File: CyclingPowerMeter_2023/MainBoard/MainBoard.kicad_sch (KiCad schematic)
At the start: 5 parts

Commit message: BLE sample code
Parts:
- removed U?: ESP32-WROOM-32, RF_Module:ESP32-WROOM-32, symbol RF_Module:ESP32-WROOM-32
- removed U?: AD7193BRUZ, SOP65P640X120-28N, symbol AD7193BRUZ:AD7193BRUZ
- added J?: Conn_01x02, symbol Connector_Generic:Conn_01x02
- added J? (x2): Conn_01x01, symbol Connector_Generic:Conn_01x01
- added MOSFET?: SSM3J332R_LF, SOT-23F_TOS, symbol SSM3J332RLF:SSM3J332R_LF
- added U?: ADS122U04IPW, PW0016A_N, symbol ADS122U04IPW:ADS122U04IPW
- added U?: Seeed_Studio_XIAO_nRF52840_Sense, symbol Seeed_Studio_XIAO_nRF52840_Sense:Seeed_Studio_XIAO_nRF52840_Sense
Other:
- moved on the sheet: C?, U?

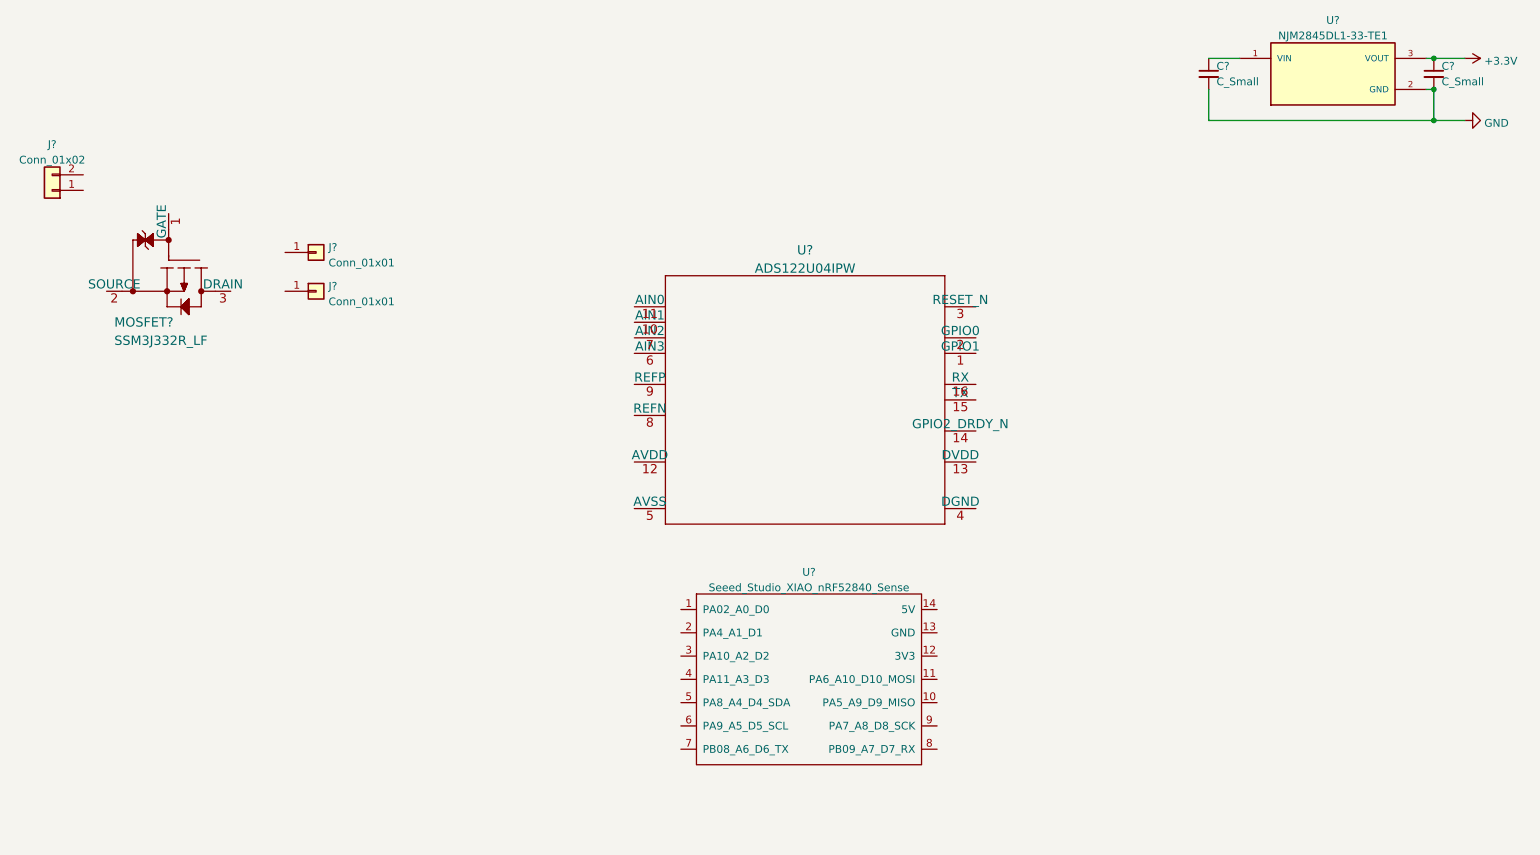
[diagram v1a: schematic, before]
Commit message: パワメの回路図が完成（暫定）
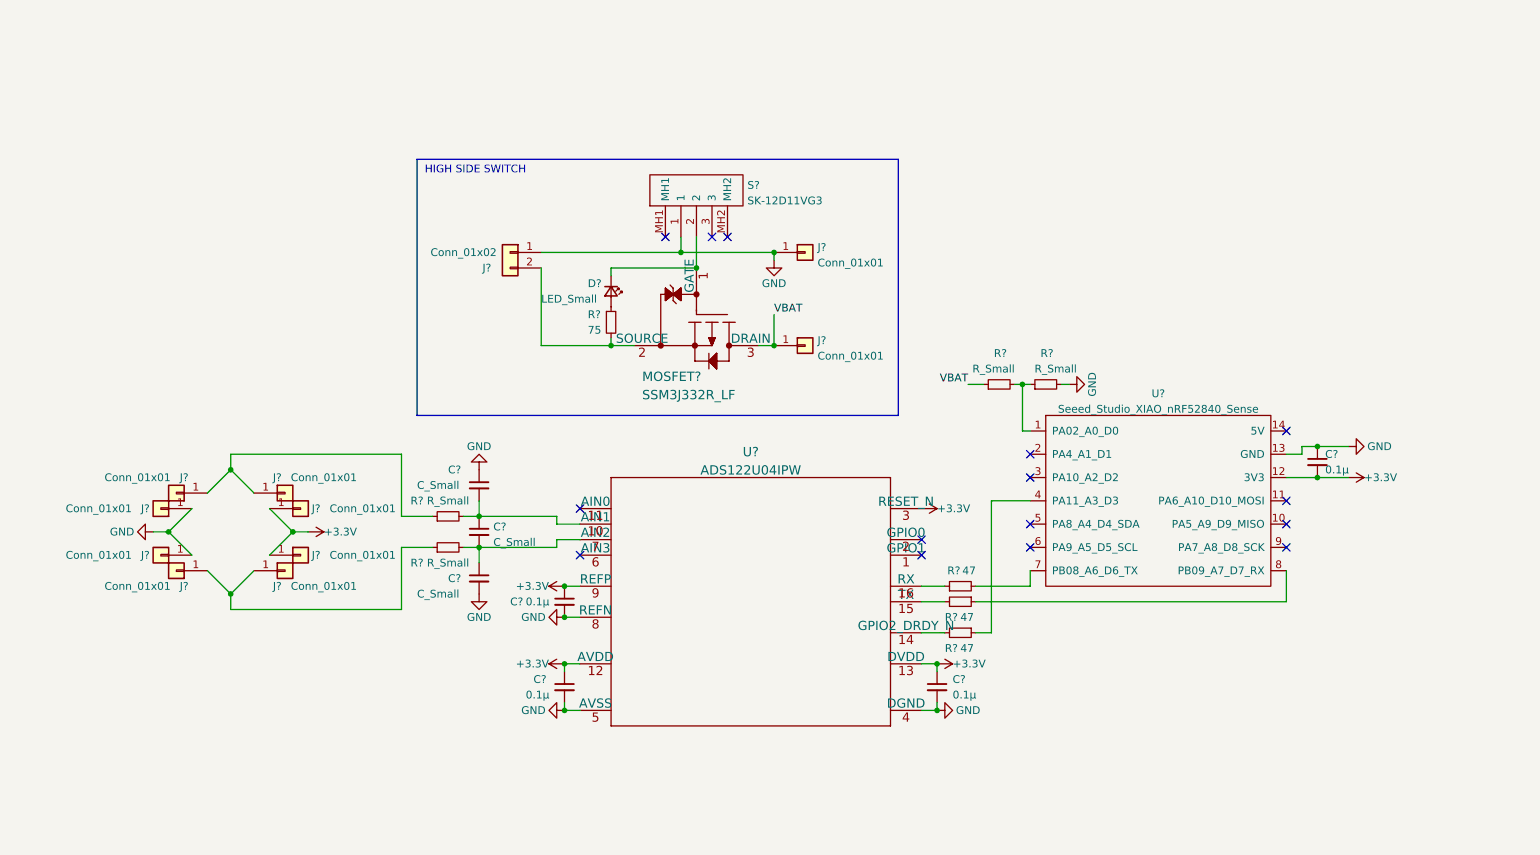
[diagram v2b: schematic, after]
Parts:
- removed C? (x2): C_Small, symbol Device:C_Small
- removed U?: NJM2845DL1-33-TE1, DPAK228P968X238-4N, symbol NJM2845DL1-33-TE1:NJM2845DL1-33-TE1
- added C? (x4): 0.1μ, symbol Device:C_Small
- added C? (x3): C_Small, symbol Device:C_Small
- added D?: LED_Small, symbol Device:LED_Small
- added J? (x8): Conn_01x01, symbol Connector_Generic:Conn_01x01
- added R? (x3): 47, symbol Device:R_Small
- added R?: 75, symbol Device:R_Small
- added R? (x4): R_Small, symbol Device:R_Small
- added S?: SK-12D11VG3, SK12D11VG3, symbol SK-12D11VG3:SK-12D11VG3
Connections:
- net +3.3V: now also U?.12 (3V3), U?.12 (AVDD), U?.13 (DVDD), U?.3 (RESET_N), U?.9 (REFP), C?.1, C?.1, C?.1, C?.2, J?.1 (Pin_1), J?.1 (Pin_1)
- net GND: now also J?.1 (Pin_1), J?.1 (Pin_1), U?.13 (GND), U?.4 (DGND), U?.5 (AVSS), U?.8 (REFN), C?.1, C?.1, C?.2, C?.2, C?.2, C?.2, J?.1 (Pin_1), J?.1 (Pin_1), R?.2, S?.1
- net at U?.10 (AIN1): now also C?.1, C?.2, R?.2
- net at U?.14 (GPIO2_DRDY_N): now also R?.2
- net at U?.15 (TX): now also R?.2
- net at U?.16 (RX): now also R?.1
- net at U?.7 (AIN2): now also C?.1, C?.2, R?.2
- net at J?.2 (Pin_2): now also MOSFET?.2 (SOURCE), R?.2
- net VBAT: now reaches J?.1 (Pin_1)
- net VBAT: now also MOSFET?.3 (DRAIN), R?.1
- net at U?.1 (PA02_A0_D0): now also R?.1, R?.2
- net at U?.4 (PA11_A3_D3): now also R?.1
- net at U?.7 (PB08_A6_D6_TX): now also R?.2
- net at U?.8 (PB09_A7_D7_RX): now also R?.1
- net at MOSFET?.1 (GATE): now also D?.1 (K), S?.2
- new net: D?.2 (A), R?.1
- new net: J?.1 (Pin_1), J?.1 (Pin_1), R?.1 (x2)
- no-connect marks 0 -> 15
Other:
- note added: "HIGH SIDE SWITCH"
- moved on the sheet: J?, MOSFET?, U?

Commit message: フットプリントを割り当て
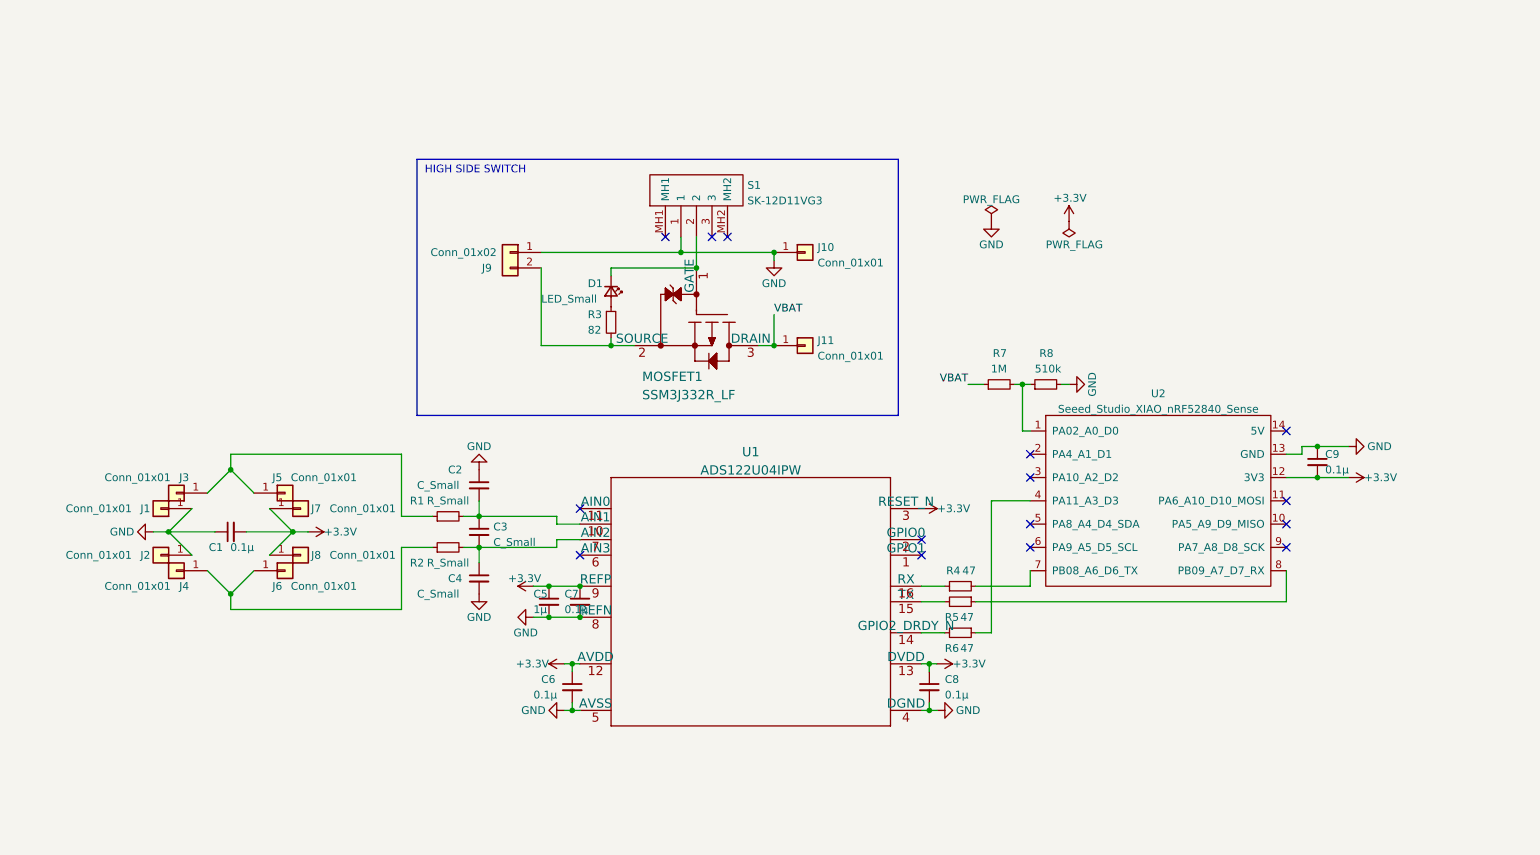
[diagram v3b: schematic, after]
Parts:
- added C1: 0.1μ, Capacitor_SMD:C_0603_1608Metric_Pad1.08x0.95mm_HandSolder, symbol Device:C_Small
- added C5: 1μ, Capacitor_SMD:C_0603_1608Metric_Pad1.08x0.95mm_HandSolder, symbol Device:C_Small
- C2, C3, C4, C6, C7, C8, C9: renamed from C?; footprint (none) -> Capacitor_SMD:C_0603_1608Metric_Pad1.08x0.95mm_HandSolder
- D1: renamed from D?; footprint (none) -> LED_SMD:LED_0603_1608Metric_Pad1.05x0.95mm_HandSolder
- J1, J2, J3, J4, J5, J6, J7, J8: renamed from J?; footprint (none) -> Connector_Wire:SolderWirePad_1x01_SMD_1x2mm
- J10, J11: renamed from J?; footprint (none) -> TestPoint:TestPoint_THTPad_4.0x4.0mm_Drill2.0mm
- J9: renamed from J?; footprint (none) -> Connector_JST:JST_PH_S2B-PH-K_1x02_P2.00mm_Horizontal
- MOSFET1: renamed from MOSFET?; footprint SOT-23F_TOS -> SSM3J332RLF:SSM3J332RLF
- R1, R2, R4, R5, R6: renamed from R?; footprint (none) -> Resistor_SMD:R_0603_1608Metric_Pad0.98x0.95mm_HandSolder
- R3: renamed from R?; value 75 -> 82; footprint (none) -> Resistor_SMD:R_0603_1608Metric_Pad0.98x0.95mm_HandSolder
- R7: renamed from R?; value R_Small -> 1M; footprint (none) -> Resistor_SMD:R_0603_1608Metric_Pad0.98x0.95mm_HandSolder
- R8: renamed from R?; value R_Small -> 510k; footprint (none) -> Resistor_SMD:R_0603_1608Metric_Pad0.98x0.95mm_HandSolder
- S1: renamed from S?; footprint SK12D11VG3 -> SK-12D11VG3:SK12D11VG3
- U1: renamed from U?; footprint PW0016A_N -> ADS122U04IPW:ADS122U04IPW
- U2: renamed from U?; footprint (none) -> Seeed_Studio_XIAO_nRF52840_Sense:Seeed_Studio_XIAO_nRF52840_Sense
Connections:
- net +3.3V: now also C1.2, C5.1
- net GND: now also C1.1, C5.2
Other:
- moved on the sheet: C6, C7, C8

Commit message: スイッチのライブラリを作成
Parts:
- removed C5: 1μ, Capacitor_SMD:C_0603_1608Metric_Pad1.08x0.95mm_HandSolder, symbol Device:C_Small
- added C? (x2): 4.7μ, Capacitor_SMD:C_0603_1608Metric_Pad1.08x0.95mm_HandSolder, symbol Device:C_Small
- added C?: 1000p, Capacitor_SMD:C_0603_1608Metric_Pad1.08x0.95mm_HandSolder, symbol Device:C_Small
- added J?: BLA05-05S30, BLA0505S30, symbol BLA05-05S30:BLA05-05S30
- C1, C7: value 0.1μ -> 0.47μ
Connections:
- net +3.3V: now also C?.2, J?.1 (+VIN_); no longer C1.2, C6.1, C7.1, J7.1 (Pin_1), J8.1 (Pin_1), U1.12 (AVDD), U1.9 (REFP)
- net GND: now also C?.1, C?.2, J?.2 (-VIN); no longer C1.1, C2.1, C4.2, C6.2, C7.2, J1.1 (Pin_1), J2.1 (Pin_1), U1.5 (AVSS), U1.8 (REFN)
- new net +5VA: C1.2, C6.1, C7.1, C?.2, J7.1 (Pin_1), J8.1 (Pin_1), J?.7 (+VOUT_), U1.12 (AVDD), U1.9 (REFP)
- new net GNDA: C1.1, C2.1, C4.2, C6.2, C7.2, C?.1, C?.1, J1.1 (Pin_1), J2.1 (Pin_1), J?.5 (-VOUT_), U1.5 (AVSS), U1.8 (REFN)
- no-connect marks 15 -> 18
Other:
- note added: "DCDC"
- moved on the sheet: C1, C2, C3, C4, C6, C7, C8, C9, D1, J1, J10, J11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

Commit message: 回路図完成
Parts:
- removed D1: LED_Small, LED_SMD:LED_0603_1608Metric_Pad1.05x0.95mm_HandSolder, symbol Device:LED_Small
- removed MOSFET1: SSM3J332R_LF, SSM3J332RLF:SSM3J332RLF, symbol SSM3J332RLF:SSM3J332R_LF
- removed R3: 82, Resistor_SMD:R_0603_1608Metric_Pad0.98x0.95mm_HandSolder, symbol Device:R_Small
- removed S1: SK-12D11VG3, SK-12D11VG3:SK12D11VG3, symbol SK-12D11VG3:SK-12D11VG3
- added SW1: RS_PRO_PCB_Slide_Switch_SPDT_Latching_3A_120V_ac_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, RS_PRO_PCB_Slide_Switch_SPDT_Latching_3A_120V_ac_Top:RS_PRO_PCB_Slide_Switch_SPDT_Latching_3A_120V_ac_Top, symbol RS_PRO_PCB_Slide_Switch_SPDT_Latching_3A_120V_ac_Top:RS_PRO_PCB_Slide_Switch_SP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
- J9: renamed from J?; footprint BLA0505S30 -> BLA05-05S30:BLA05-05S30
- gave numbers to parts that had none: 3
- renumbered C8 to C10, C9 to C11, C1 to C2, C2 to C5, C3 to C6, C4 to C7, C6 to C8, C7 to C9, J9 to J10, J10 to J11, J11 to J12, R4 to R3, R5 to R4, R6 to R5, R7 to R6, R8 to R7
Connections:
- net GND: now also J12.1 (Pin_1); no longer J11.1 (Pin_1)
- net VBAT: now also J11.1 (Pin_1), SW1.2; no longer J12.1 (Pin_1)
- net at J10.2 (Pin_2): now also SW1.1
- no-connect marks 18 -> 16
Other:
- note added: "SWITCH"
- note removed: "HIGH SIDE SWITCH"
- moved on the sheet: C1, C3, C4, J10, J11, J12, J9

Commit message: 基板5/10
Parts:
- removed J10: Conn_01x02, Connector_JST:JST_PH_S2B-PH-K_1x02_P2.00mm_Horizontal, symbol Connector_Generic:Conn_01x02
- added J10: S2B-PH-SM4-TB_LF__SN_, S2B-PH-SM4-TB:S2B-PH-SM4-TB, symbol S2B-PH-SM4-TB:S2B-PH-SM4-TB_LF__SN_
- added S1: B3AL-1002P-MS, B3AL-1002P-MS:B3AL-1002P-MS, symbol B3AL-1002P-MS:B3AL-1002P-MS
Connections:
- net GND: now also J10.1, S1.1
- net at SW1.1: now also J10.2
- net at U2.2 (PA4_A1_D1): now also S1.2
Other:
- moved on the sheet: J11, J12, SW1

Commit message: 配線進捗5割
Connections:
- net at R5.1: now also U2.2 (PA4_A1_D1); no longer U2.4 (PA11_A3_D3)
- net at S1.2: now also U2.4 (PA11_A3_D3); no longer U2.2 (PA4_A1_D1)
- no-connect marks 16 -> 17
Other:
- moved on the sheet: S1
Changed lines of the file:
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@@
   (junction (at 48.26 60.96) (diameter 0) (color 0 0 0 0)
   )
+  (no_connect (at 119.38 91.44))
   (no_connect (at 149.86 48.26))
   (no_connect (at 193.04 90.17))
@@
     (stroke (width 0) (type default) (color 0 0 0 0))
   )
+  (wire (pts (xy 190.5 72.39) (xy 190.5 82.55))
+    (stroke (width 0) (type default) (color 0 0 0 0))
+  )
   (wire (pts (xy 92.71 55.88) (xy 99.06 55.88))
     (stroke (width 0) (type default) (color 0 0 0 0))
@@
     (stroke (width 0) (type default) (color 0 0 0 0))
   )
-  (wire (pts (xy 189.23 74.93) (xy 193.04 74.93))
-    (stroke (width 0) (type default) (color 0 0 0 0))
-  )
   (wire (pts (xy 191.77 71.12) (xy 193.04 71.12))
     (stroke (width 0) (type default) (color 0 0 0 0))
@@
     (stroke (width 0) (type default) (color 0 0 0 0))
   )
-  (wire (pts (xy 186.69 104.14) (xy 186.69 82.55))
-    (stroke (width 0) (type default) (color 0 0 0 0))
-  )
   (wire (pts (xy 240.03 78.74) (xy 245.11 78.74))
     (stroke (width 0) (type default) (color 0 0 0 0))
@@
     (stroke (width 0) (type default) (color 0 0 0 0))
   )
+  (wire (pts (xy 190.5 82.55) (xy 193.04 82.55))
+    (stroke (width 0) (type default) (color 0 0 0 0))
+  )
   (wire (pts (xy 62.23 74.93) (xy 90.17 74.93))
     (stroke (width 0) (type default) (color 0 0 0 0))
@@
     (stroke (width 0) (type default) (color 0 0 0 0))
   )
-  (wire (pts (xy 186.69 82.55) (xy 193.04 82.55))
+  (wire (pts (xy 186.69 74.93) (xy 186.69 104.14))
     (stroke (width 0) (type default) (color 0 0 0 0))
   )
@@
     (stroke (width 0) (type default) (color 0 0 0 0))
   )
+  (wire (pts (xy 187.96 72.39) (xy 190.5 72.39))
+    (stroke (width 0) (type default) (color 0 0 0 0))
+  )
   (wire (pts (xy 147.32 48.26) (xy 147.32 50.8))
     (stroke (width 0) (type default) (color 0 0 0 0))
@@
   )
   (wire (pts (xy 118.11 109.22) (xy 119.38 109.22))
+    (stroke (width 0) (type default) (color 0 0 0 0))
+  )
+  (wire (pts (xy 186.69 74.93) (xy 193.04 74.93))
     (stroke (width 0) (type default) (color 0 0 0 0))
   )
@@
     (pin "7")
   )
-  (symbol (lib_id "power:GND") (at 189.23 77.47 0) (unit 1)
-    (in_bom yes) (on_board yes)
-    (property "Reference" "#PWR018" (id 0) (at 189.23 83.82 0)
-      (effects (font (size 1.27 1.27)) hide)
-    )
-    (property "Value" "GND" (id 1) (at 189.23 81.28 0))
-    (property "Footprint" "" (id 2) (at 189.23 77.47 0)
-      (effects (font (size 1.27 1.27)) hide)
-    )
-    (property "Datasheet" "" (id 3) (at 189.23 77.47 0)
+  (symbol (lib_id "power:GND") (at 187.96 69.85 0) (mirror x) (unit 1)
+    (in_bom yes) (on_board yes)
+    (property "Reference" "#PWR018" (id 0) (at 187.96 63.5 0)
+      (effects (font (size 1.27 1.27)) hide)
+    )
+    (property "Value" "GND" (id 1) (at 187.96 66.04 0))
+    (property "Footprint" "" (id 2) (at 187.96 69.85 0)
+      (effects (font (size 1.27 1.27)) hide)
+    )
+    (property "Datasheet" "" (id 3) (at 187.96 69.85 0)
       (effects (font (size 1.27 1.27)) hide)
     )
@@
     (pin "1")
   )
-  (symbol (lib_id "B3AL-1002P-MS:B3AL-1002P-MS") (at 189.23 74.93 0) (mirror y) (unit 1)
+  (symbol (lib_id "B3AL-1002P-MS:B3AL-1002P-MS") (at 187.96 72.39 180) (unit 1)
     (in_bom yes) (on_board yes) (fields_autoplaced)
-    (property "Reference" "S1" (id 0) (at 179.07 68.741 0))
-    (property "Value" "B3AL-1002P-MS" (id 1) (at 179.07 71.2779 0))
-    (property "Footprint" "B3AL-1002P-MS:B3AL-1002P-MS" (id 2) (at 172.72 72.39 0)
-      (effects (font (size 1.27 1.27)) (justify left) hide)
-    )
-    (property "Datasheet" "https://componentsearchengine.com/Datasheets/1/B3AL-1002P-MS.pdf" (id 3) (at 172.72 74.93 0)
-      (effects (font (size 1.27 1.27)) (justify left) hide)
-    )
-    (property "Description" "OMRON ELECTRONIC COMPONENTS - B3AL-1002P-MS - TACTILE SWITCH, SPST-NO, 0.05A, 16V, SMT" (id 4) (at 172.72 77.47 0)
-      (effects (font (size 1.27 1.27)) (justify left) hide)
-    )
-    (property "Height" "5.4" (id 5) (at 172.72 80.01 0)
-      (effects (font (size 1.27 1.27)) (justify left) hide)
-    )
-    (property "Manufacturer_Name" "Omron Electronics" (id 6) (at 172.72 82.55 0)
-      (effects (font (size 1.27 1.27)) (justify left) hide)
-    )
-    (property "Manufacturer_Part_Number" "B3AL-1002P-MS" (id 7) (at 172.72 85.09 0)
-      (effects (font (size 1.27 1.27)) (justify left) hide)
-    )
-    (property "Mouser Part Number" "653-B3AL-1002P-MS" (id 8) (at 172.72 87.63 0)
-      (effects (font (size 1.27 1.27)) (justify left) hide)
-    )
-    (property "Mouser Price/Stock" "https://www.mouser.co.uk/ProductDetail/Omron-Electronics/B3AL-1002P-MS?qs=HXFqYaX1Q2yMcMO0j50f3A%3D%3D" (id 9) (at 172.72 90.17 0)
-      (effects (font (size 1.27 1.27)) (justify left) hide)
-    )
-    (property "Arrow Part Number" "B3AL-1002P-MS" (id 10) (at 172.72 92.71 0)
-      (effects (font (size 1.27 1.27)) (justify left) hide)
-    )
-    (property "Arrow Price/Stock" "https://www.arrow.com/en/products/b3al-1002p-ms/omron?region=nac" (id 11) (at 172.72 95.25 0)
-      (effects (font (size 1.27 1.27)) (justify left) hide)
-    )
-    (property "Mouser Testing Part Number" "" (id 12) (at 172.72 97.79 0)
-      (effects (font (size 1.27 1.27)) (justify left) hide)
-    )
-    (property "Mouser Testing Price/Stock" "" (id 13) (at 172.72 100.33 0)
-      (effects (font (size 1.27 1.27)) (justify left) hide)
-    )
+    (property "Reference" "S1" (id 0) (at 177.8 78.579 0))
+    (property "Value" "B3AL-1002P-MS" (id 1) (at 177.8 76.0421 0))
+    (property "Footprint" "B3AL-1002P-MS:B3AL-1002P-MS" (id 2) (at 171.45 74.93 0)
+      (effects (font (size 1.27 1.27)) (justify left) hide)
+    )
+    (property "Datasheet" "https://componentsearchengine.com/Datasheets/1/B3AL-1002P-MS.pdf" (id 3) (at 171.45 72.39 0)
+      (effects (font (size 1.27 1.27)) (justify left) hide)
+    )
+    (property "Description" "OMRON ELECTRONIC COMPONENTS - B3AL-1002P-MS - TACTILE SWITCH, SPST-NO, 0.05A, 16V, SMT" (id 4) (at 171.45 69.85 0)
+      (effects (font (size 1.27 1.27)) (justify left) hide)
+    )
+    (property "Height" "5.4" (id 5) (at 171.45 67.31 0)
+      (effects (font (size 1.27 1.27)) (justify left) hide)
+    )
+    (property "Manufacturer_Name" "Omron Electronics" (id 6) (at 171.45 64.77 0)
+      (effects (font (size 1.27 1.27)) (justify left) hide)
+    )
+    (property "Manufacturer_Part_Number" "B3AL-1002P-MS" (id 7) (at 171.45 62.23 0)
+      (effects (font (size 1.27 1.27)) (justify left) hide)
+    )
+    (property "Mouser Part Number" "653-B3AL-1002P-MS" (id 8) (at 171.45 59.69 0)
+      (effects (font (size 1.27 1.27)) (justify left) hide)
+    )
+    (property "Mouser Price/Stock" "https://www.mouser.co.uk/ProductDetail/Omron-Electronics/B3AL-1002P-MS?qs=HXFqYaX1Q2yMcMO0j50f3A%3D%3D" (id 9) (at 171.45 57.15 0)
+      (effects (font (size 1.27 1.27)) (justify left) hide)
+    )
+    (property "Arrow Part Number" "B3AL-1002P-MS" (id 10) (at 171.45 54.61 0)
+      (effects (font (size 1.27 1.27)) (justify left) hide)
+    )
+    (property "Arrow Price/Stock" "https://www.arrow.com/en/products/b3al-1002p-ms/omron?region=nac" (id 11) (at 171.45 52.07 0)
+      (effects (font (size 1.27 1.27)) (justify left) hide)
+    )
+    (property "Mouser Testing Part Number" "" (id 12) (at 171.45 49.53 0)
+      (effects (font (size 1.27 1.27)) (justify left) hide)
+    )
+    (property "Mouser Testing Price/Stock" "" (id 13) (at 171.45 46.99 0)
+      (effects (font (size 1.27 1.27)) (justify left) hide)
+    )
